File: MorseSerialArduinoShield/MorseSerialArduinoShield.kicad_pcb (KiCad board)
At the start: 2 copper layers, 77.5 x 58.4 mm, 12 parts, among them U1 SC39-11SRWA

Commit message: re done efge cuts and values added
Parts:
- R1 1k: renamed from R1
- R2 1K: renamed from R2
- R3 1K: renamed from R3
- R4 1K: renamed from R4
- R5 1K: renamed from R5
- R6 1K: renamed from R6
- R7 1K: renamed from R7
- R8 1K: renamed from R8
- RV1 220ohm: renamed from RV1
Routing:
- net Net-(A1-Pad22): track 66.4 -> 72.6 mm
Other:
- board size 77.5 x 58.4 mm -> 76.2 x 54.6 mm
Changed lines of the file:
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@@
   (general
     (thickness 1.6)
-    (drawings 24)
-    (tracks 74)
+    (drawings 38)
+    (tracks 77)
     (zones 0)
     (modules 12)
@@
     (descr "Potentiometer, vertical, Trimmer, RM-065 http://www.runtron.com/down/PDF%20Datasheet/Carbon%20Film%20Potentiometer/RM065%20RM063.pdf")
     (tags "Potentiometer Trimmer RM-065")
-    (fp_text reference RV1 (at 2.6 -2.5) (layer F.SilkS)
+    (fp_text reference "RV1 220ohm" (at 2.6 -2.5) (layer F.SilkS)
       (effects (font (size 1 1) (thickness 0.15)))
     )
@@
     (descr "Resistor, Axial_DIN0309 series, Axial, Horizontal, pin pitch=12.7mm, 0.5W = 1/2W, length*diameter=9*3.2mm^2, http://cdn-reichelt.de/documents/datenblatt/B400/1_4W%23YAG.pdf")
     (tags "Resistor Axial_DIN0309 series Axial Horizontal pin pitch 12.7mm 0.5W = 1/2W length 9mm diameter 3.2mm")
-    (fp_text reference R7 (at 6.35 -2.72) (layer F.SilkS)
+    (fp_text reference "R7 1K" (at 6.35 -2.72) (layer F.SilkS)
       (effects (font (size 1 1) (thickness 0.15)))
     )
@@
     (descr "Resistor, Axial_DIN0309 series, Axial, Horizontal, pin pitch=12.7mm, 0.5W = 1/2W, length*diameter=9*3.2mm^2, http://cdn-reichelt.de/documents/datenblatt/B400/1_4W%23YAG.pdf")
     (tags "Resistor Axial_DIN0309 series Axial Horizontal pin pitch 12.7mm 0.5W = 1/2W length 9mm diameter 3.2mm")
-    (fp_text reference R8 (at 6.35 -2.72) (layer F.SilkS)
+    (fp_text reference "R8 1K" (at 6.35 -2.72) (layer F.SilkS)
       (effects (font (size 1 1) (thickness 0.15)))
     )
@@
       (effects (font (size 1 1) (thickness 0.15)))
     )
-    (fp_text user %R (at 6.35 0) (layer F.Fab)
+    (fp_text user %R (at 6.35 0 90) (layer F.Fab)
       (effects (font (size 1 1) (thickness 0.15)))
     )
@@
     (descr "Resistor, Axial_DIN0309 series, Axial, Horizontal, pin pitch=12.7mm, 0.5W = 1/2W, length*diameter=9*3.2mm^2, http://cdn-reichelt.de/documents/datenblatt/B400/1_4W%23YAG.pdf")
     (tags "Resistor Axial_DIN0309 series Axial Horizontal pin pitch 12.7mm 0.5W = 1/2W length 9mm diameter 3.2mm")
-    (fp_text reference R6 (at 6.35 -2.72) (layer F.SilkS)
+    (fp_text reference "R6 1K" (at 6.35 -2.72) (layer F.SilkS)
       (effects (font (size 1 1) (thickness 0.15)))
     )
@@
     (descr "Resistor, Axial_DIN0309 series, Axial, Horizontal, pin pitch=12.7mm, 0.5W = 1/2W, length*diameter=9*3.2mm^2, http://cdn-reichelt.de/documents/datenblatt/B400/1_4W%23YAG.pdf")
     (tags "Resistor Axial_DIN0309 series Axial Horizontal pin pitch 12.7mm 0.5W = 1/2W length 9mm diameter 3.2mm")
-    (fp_text reference R5 (at 6.35 -2.72) (layer F.SilkS)
+    (fp_text reference "R5 1K" (at 6.35 -2.72) (layer F.SilkS)
       (effects (font (size 1 1) (thickness 0.15)))
     )
@@
     (descr "Resistor, Axial_DIN0309 series, Axial, Horizontal, pin pitch=12.7mm, 0.5W = 1/2W, length*diameter=9*3.2mm^2, http://cdn-reichelt.de/documents/datenblatt/B400/1_4W%23YAG.pdf")
     (tags "Resistor Axial_DIN0309 series Axial Horizontal pin pitch 12.7mm 0.5W = 1/2W length 9mm diameter 3.2mm")
-    (fp_text reference R4 (at 6.35 -2.72) (layer F.SilkS)
+    (fp_text reference "R4 1K" (at 6.35 -2.72) (layer F.SilkS)
       (effects (font (size 1 1) (thickness 0.15)))
     )
@@
     (descr "Resistor, Axial_DIN0309 series, Axial, Horizontal, pin pitch=12.7mm, 0.5W = 1/2W, length*diameter=9*3.2mm^2, http://cdn-reichelt.de/documents/datenblatt/B400/1_4W%23YAG.pdf")
     (tags "Resistor Axial_DIN0309 series Axial Horizontal pin pitch 12.7mm 0.5W = 1/2W length 9mm diameter 3.2mm")
-    (fp_text reference R3 (at 6.35 -2.72) (layer F.SilkS)
+    (fp_text reference "R3 1K" (at 6.35 -2.72) (layer F.SilkS)
       (effects (font (size 1 1) (thickness 0.15)))
     )
@@
     (descr "Resistor, Axial_DIN0309 series, Axial, Horizontal, pin pitch=12.7mm, 0.5W = 1/2W, length*diameter=9*3.2mm^2, http://cdn-reichelt.de/documents/datenblatt/B400/1_4W%23YAG.pdf")
     (tags "Resistor Axial_DIN0309 series Axial Horizontal pin pitch 12.7mm 0.5W = 1/2W length 9mm diameter 3.2mm")
-    (fp_text reference R2 (at 6.35 -2.72) (layer F.SilkS)
+    (fp_text reference "R2 1K" (at 6.35 -2.72) (layer F.SilkS)
       (effects (font (size 1 1) (thickness 0.15)))
     )
@@
     (descr "Resistor, Axial_DIN0309 series, Axial, Horizontal, pin pitch=12.7mm, 0.5W = 1/2W, length*diameter=9*3.2mm^2, http://cdn-reichelt.de/documents/datenblatt/B400/1_4W%23YAG.pdf")
     (tags "Resistor Axial_DIN0309 series Axial Horizontal pin pitch 12.7mm 0.5W = 1/2W length 9mm diameter 3.2mm")
-    (fp_text reference R1 (at 6.35 -2.72) (layer F.SilkS)
+    (fp_text reference "R1 1k" (at 6.35 -2.72) (layer F.SilkS)
       (effects (font (size 1 1) (thickness 0.15)))
     )
@@
     )
   )
+  (gr_line (start 110.363 74.93) (end 110.998 74.93) (layer Edge.Cuts) (width 0.15))
+  (gr_line (start 110.363 84.455) (end 110.363 74.93) (layer Edge.Cuts) (width 0.15))
+  (gr_line (start 104.013 84.455) (end 110.363 84.455) (layer Edge.Cuts) (width 0.15))
+  (gr_line (start 104.013 97.155) (end 104.013 84.455) (layer Edge.Cuts) (width 0.15))
+  (gr_line (start 110.363 97.155) (end 104.013 97.155) (layer Edge.Cuts) (width 0.15))
+  (gr_line (start 110.363 116.205) (end 110.363 97.155) (layer Edge.Cuts) (width 0.15))
+  (gr_line (start 108.458 116.205) (end 110.363 116.205) (layer Edge.Cuts) (width 0.15))
+  (gr_line (start 108.458 126.365) (end 108.458 116.205) (layer Edge.Cuts) (width 0.15))
+  (gr_line (start 110.363 126.365) (end 108.458 126.365) (layer Edge.Cuts) (width 0.15))
+  (gr_line (start 110.363 129.54) (end 110.363 126.365) (layer Edge.Cuts) (width 0.15))
+  (gr_line (start 177.673 129.54) (end 110.363 129.54) (layer Edge.Cuts) (width 0.15))
+  (gr_line (start 177.673 126.365) (end 177.673 129.54) (layer Edge.Cuts) (width 0.15))
+  (gr_line (start 180.213 123.825) (end 177.673 126.365) (layer Edge.Cuts) (width 0.15))
+  (gr_line (start 180.213 90.805) (end 180.213 123.825) (layer Edge.Cuts) (width 0.15))
+  (gr_line (start 177.673 88.265) (end 180.213 90.805) (layer Edge.Cuts) (width 0.15))
+  (gr_line (start 177.673 76.835) (end 177.673 88.265) (layer Edge.Cuts) (width 0.15))
+  (gr_line (start 175.768 74.93) (end 177.673 76.835) (layer Edge.Cuts) (width 0.15))
+  (gr_line (start 110.998 74.93) (end 175.768 74.93) (layer Edge.Cuts) (width 0.15))
   (gr_line (start 110.998 128.905) (end 177.038 128.905) (layer F.SilkS) (width 0.15))
   (gr_line (start 110.998 125.73) (end 110.998 128.905) (layer F.SilkS) (width 0.15))
@@
   (gr_line (start 177.038 126.365) (end 179.578 123.825) (layer F.SilkS) (width 0.15))
   (gr_line (start 177.038 128.905) (end 177.038 126.365) (layer F.SilkS) (width 0.15))
-  (gr_line (start 180.848 73.025) (end 180.848 131.445) (layer Edge.Cuts) (width 0.1))
-  (gr_line (start 103.378 73.025) (end 180.848 73.025) (layer Edge.Cuts) (width 0.1))
-  (gr_line (start 103.378 131.445) (end 103.378 73.025) (layer Edge.Cuts) (width 0.1))
-  (gr_line (start 180.848 131.445) (end 103.378 131.445) (layer Edge.Cuts) (width 0.1))
   (gr_text "Arduino Morse Code\nBeep and Display\nVersion 1.0" (at 165.608 86.995) (layer F.SilkS)
     (effects (font (size 1 1) (thickness 0.15)))
@@
   (segment (start 139.958 90.805) (end 152.658 78.105) (width 0.25) (layer F.Cu) (net 17))
   (segment (start 131.318 90.805) (end 139.958 90.805) (width 0.25) (layer F.Cu) (net 17))
-  (segment (start 122.428 116.205) (end 122.428 113.665) (width 0.25) (layer F.Cu) (net 19))
-  (segment (start 122.428 113.665) (end 132.588 103.505) (width 0.25) (layer F.Cu) (net 19))
-  (segment (start 132.588 103.505) (end 132.588 92.075) (width 0.25) (layer F.Cu) (net 19))
-  (segment (start 132.588 92.075) (end 156.718 92.075) (width 0.25) (layer F.Cu) (net 19))
-  (segment (start 156.718 92.075) (end 156.718 78.105) (width 0.25) (layer F.Cu) (net 19))
+  (segment (start 156.718 95.885) (end 156.718 78.105) (width 0.25) (layer F.Cu) (net 19))
+  (segment (start 144.018 95.885) (end 156.718 95.885) (width 0.25) (layer F.Cu) (net 19))
+  (segment (start 139.573 91.44) (end 144.018 95.885) (width 0.25) (layer F.Cu) (net 19))
+  (segment (start 133.223 92.075) (end 133.858 91.44) (width 0.25) (layer F.Cu) (net 19))
+  (segment (start 122.428 116.205) (end 123.55937 116.205) (width 0.25) (layer F.Cu) (net 19))
+  (segment (start 133.223 106.54137) (end 133.223 92.075) (width 0.25) (layer F.Cu) (net 19))
+  (segment (start 123.55937 116.205) (end 133.223 106.54137) (width 0.25) (layer F.Cu) (net 19))
+  (segment (start 133.858 91.44) (end 139.573 91.44) (width 0.25) (layer F.Cu) (net 19))
   (segment (start 173.228 109.855) (end 163.068 99.695) (width 0.25) (layer F.Cu) (net 21))
   (segment (start 163.068 81.915) (end 159.258 78.105) (width 0.25) (layer F.Cu) (net 21))

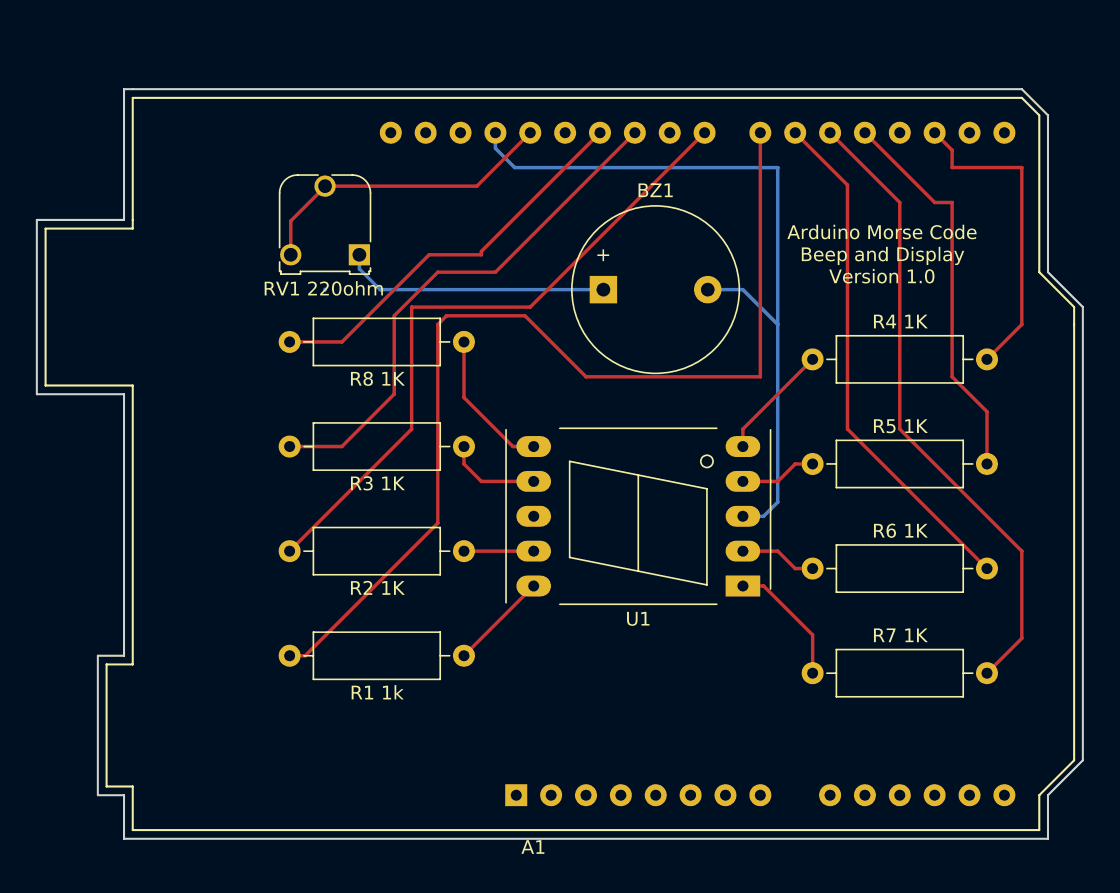
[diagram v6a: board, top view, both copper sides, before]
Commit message: Untested Bluetooth variant using HC-05
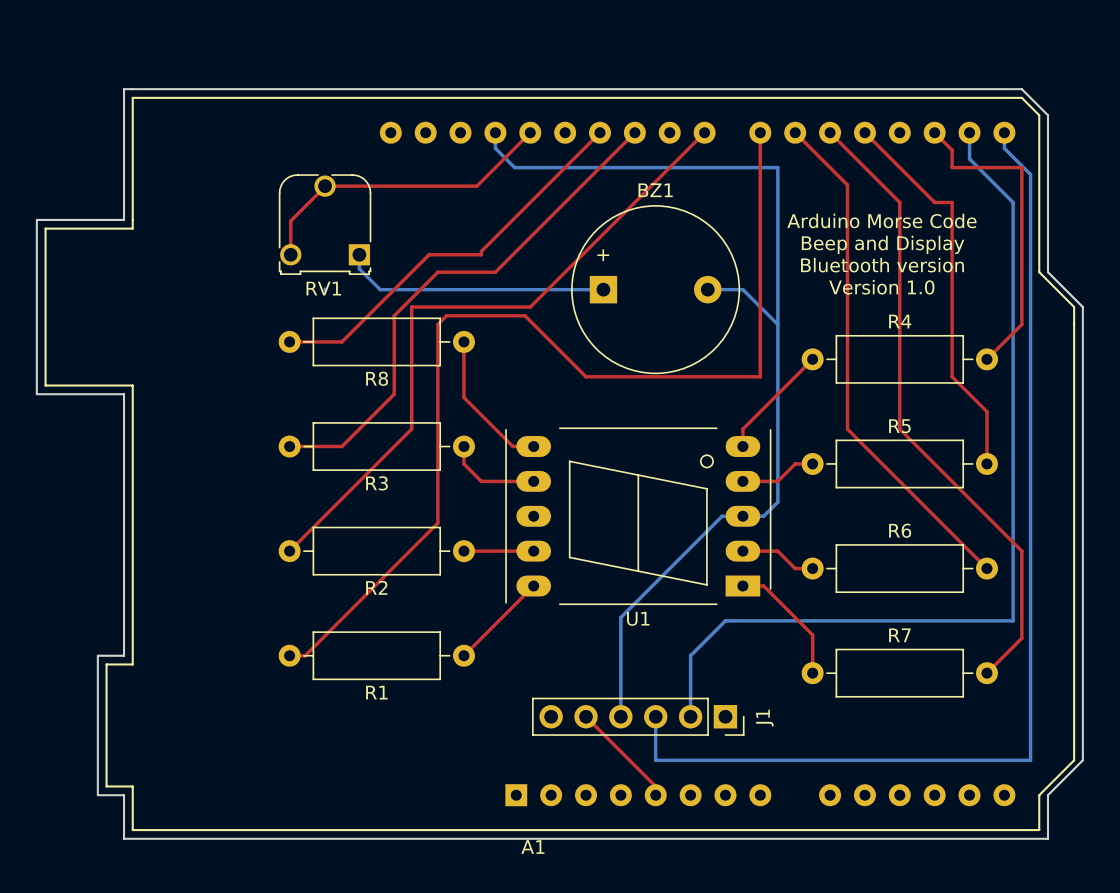
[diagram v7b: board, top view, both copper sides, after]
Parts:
- added J1: HC_05, Connector_PinSocket_2.54mm:PinSocket_1x06_P2.54mm_Vertical, F.Cu at (154.2, 120.7)
- R1: renamed from R1 1k
- R2: renamed from R2 1K
- R3: renamed from R3 1K
- R4: renamed from R4 1K
- R5: renamed from R5 1K
- R6: renamed from R6 1K
- R7: renamed from R7 1K
- R8: renamed from R8 1K
- RV1: renamed from RV1 220ohm
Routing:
- net Net-(A1-Pad15): track 0.00 -> 77.0 mm
- net Net-(A1-Pad16): track 0.00 -> 65.9 mm
- net GND: track 55.8 -> 74.9 mm
- net Net-(A1-Pad5): track 0.00 -> 7.82 mm
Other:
- board text added: "Arduino Morse Code Beep and Display Bluetooth version Version 1.0"
- board text removed: "Arduino Morse Code Beep and Display Version 1.0"
